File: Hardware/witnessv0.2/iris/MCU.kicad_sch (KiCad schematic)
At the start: 36 parts, among them J1 Conn_01x02, J4 Conn_01x02, U1 ESP32-S3FN8, U8 W25N01KVZEIR, Y1 F322540MUBCE2O

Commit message: iris rework
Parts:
- removed C28, C29: 100n, Capacitor_SMD:C_0402_1005Metric, symbol Device:C_Small
- removed L4: 10n, Inductor_SMD:L_0805_2012Metric, symbol Device:L_Small
- BZ1: footprint Buzzer_Beeper:Buzzer_Murata_PKMCS0909E -> Witness:OWMB-505020S-40-12D
- U8: LCSC_Part (none) -> C22472329
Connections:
- net SPI3_IO2 is gone; now on net SPI2_IO1: U8.2 (DO/IO_{1})
- net +3V3: now also U1.2 (VDD3P3), U1.3 (VDD3P3)
- net BUZZER: now also U1.36 (SPICLK_N)
- net FLASH_CS: now also U1.15 (GPIO10)
- net GND: now also U8.9 (EP)
- net LED_B: now also U1.37 (SPICLK_P)
- net LED_G: now also U1.48 (MTMS)
- net LED_R: now also U1.47 (MTDI)
- net SPI2_CLK: now also U1.17 (GPIO12)
- net SPI2_IO1: now also U1.18 (GPIO13); no longer U8.5 (DI/IO_{0})
- net RXD_MCU: now reaches U1.10 (GPIO5)
- net RAD_RST: now reaches U1.11 (GPIO6)
- net LSM_INT1: now reaches U1.12 (GPIO7)
- net LSM_INT2: now reaches U1.13 (GPIO8)
- net SPI2_IO3: now reaches U1.14 (GPIO9)
- net SPI2_IO3: now also U8.7 (~{HOLD}/~{RESET}/IO_{3})
- net SPI2_IO0: now reaches U1.16 (GPIO11)
- net SPI2_IO0: now also U8.5 (DI/IO_{0})
- net SPI2_IO2: now reaches U1.19 (GPIO14)
- net SPI2_IO2: now also U8.3 (~{WP}/IO_{2})
- net SPI3_SCLK: now reaches U1.21 (XTAL_32K_P)
- net RAD_CS: now reaches U1.22 (XTAL_32K_N)
- net SPI3_COPI: now reaches U1.23 (GPIO17)
- net SPI3_CIPO: now reaches U1.24 (GPIO18)
- net MS56_CS: now reaches U1.27 (GPIO21)
- net I2C_SDA: now reaches U1.38 (GPIO33)
- net I2C_SCL: now reaches U1.39 (GPIO34)
- net LSM_CS: now reaches U1.40 (GPIO35)
- net CANTX: now reaches U1.41 (GPIO36)
- net CANRX: now reaches U1.42 (GPIO37)
- net GPIO: now reaches U1.43 (GPIO38)
- net RAD_BUSY: now reaches U1.44 (MTCK)
- net RAD_RF_EN: now reaches U1.45 (MTDO)
- net VSENSE: now reaches U1.6 (GPIO1)
- net RAD_DIO1: now reaches U1.7 (GPIO2)
- net TXD_MCU: now reaches U1.9 (GPIO4)
- removed net SPI3_IO3: U8.3 (~{WP}/IO_{2}), U8.7 (~{HOLD}/~{RESET}/IO_{3})
- no-connect marks 7 -> 10
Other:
- moved on the sheet: C35, R30, R31

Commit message: trying to make cam board
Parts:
- removed AE1: Antenna_Shield, Connector_Coaxial:U.FL_Molex_MCRF_73412-0110_Vertical, symbol Device:Antenna_Shield
- removed C32, C33, C35: 100n, Capacitor_SMD:C_0402_1005Metric, symbol Device:C_Small
- removed L5: L_Small, Inductor_SMD:L_0402_1005Metric, symbol Device:L_Small
- removed U8: W25N01KVZEIR, Package_SON:WSON-8-1EP_8x6mm_P1.27mm_EP3.4x4.3mm, symbol Witness:W25N01KVZEIR
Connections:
- net FLASH_CS: no longer names the net of U1.15 (GPIO10)
- net GPIO: no longer names the net of U1.43 (GPIO38)
- net RAD_BUSY: no longer names the net of U1.44 (MTCK)
- net RAD_RF_EN: no longer names the net of U1.45 (MTDO)
- net SPI2_CLK: no longer names the net of U1.17 (GPIO12)
- net SPI2_IO0: no longer names the net of U1.16 (GPIO11)
- net SPI2_IO1: no longer names the net of U1.18 (GPIO13)
- net SPI2_IO2: no longer names the net of U1.19 (GPIO14)
- net SPI2_IO3: no longer names the net of U1.14 (GPIO9)

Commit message: lots of iris work
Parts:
- removed U1: ESP32-S3FN8, Package_DFN_QFN:QFN-56-1EP_7x7mm_P0.4mm_EP4x4mm, symbol MCU_Espressif:ESP32-S3
- added U7: ESP32-C3, Package_DFN_QFN:QFN-32-1EP_5x5mm_P0.5mm_EP3.7x3.7mm, symbol MCU_Espressif:ESP32-C3
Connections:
- net +3V3: now also U7.11 (VDD3P3_RTC), U7.17 (VDD3P3_CPU), U7.18 (VDD_SPI), U7.2 (VDD3P3), U7.3 (VDD3P3), U7.31 (VDDA), U7.32 (VDDA)
- net GND: now also U7.33 (GND)
- net RST: now also U7.7 (CHIP_EN)
- net VSENSE: now also U7.6 (GPIO2)
- net XIN: now also U7.30 (XTAL_P)
- new net CS1: U7.4 (XTAL_32K_P)
- new net CS2: U7.5 (XTAL_32K_N)
- new net CS3: U7.8 (GPIO3)
- new net CS4: U7.9 (MTMS)
- no-connect marks 10 -> 4
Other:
- moved on the sheet: C26, C27, C3, C30, C31, C4, C5, C6, R30, R31

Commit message: push for andrew
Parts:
- removed BZ1: Buzzer, Witness:OWMB-505020S-40-12D, symbol Device:Buzzer
- removed R26, R27, R28, R29: 4.7k, Resistor_SMD:R_0402_1005Metric, symbol Device:R_Small
- R24: now not fitted
- R25: now fitted
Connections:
- net CS1 is gone; now on net VSENSE: U7.4 (XTAL_32K_P)
- net CS2 is gone; now on net CANTX: U7.5 (XTAL_32K_N)
- net CS3 is gone; now on net CANRX: U7.8 (GPIO3)
- net CS4 is gone; now on net SDA: U7.9 (MTMS)
- net GPIO46 is gone; now on net BUZZER: R24.2, R25.1
- net LED_B: now also U7.16 (GPIO10)
- net LED_G: now also U7.15 (GPIO9)
- net LED_R: now also U7.6 (GPIO2)
- net RXD1_MCU: now also U7.13 (MTDO)
- net SCL: now also U7.10 (MTDI)
- net TXD1_MCU: now also U7.12 (MTCK)
- net VSENSE: no longer U7.6 (GPIO2)
- net at R30.2: now also U7.25 (GPIO18)
- net at R31.2: now also U7.26 (GPIO19)
- net BUTTON: now reaches U7.14 (GPIO8)
- net RXD0_MCU: now reaches U7.27 (U0RXD)
- net TXD0_MCU: now reaches U7.28 (U0TXD)
- net GPIO0 renamed GPIO9
- no-connect marks 4 -> 8
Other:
- moved on the sheet: R30, R31

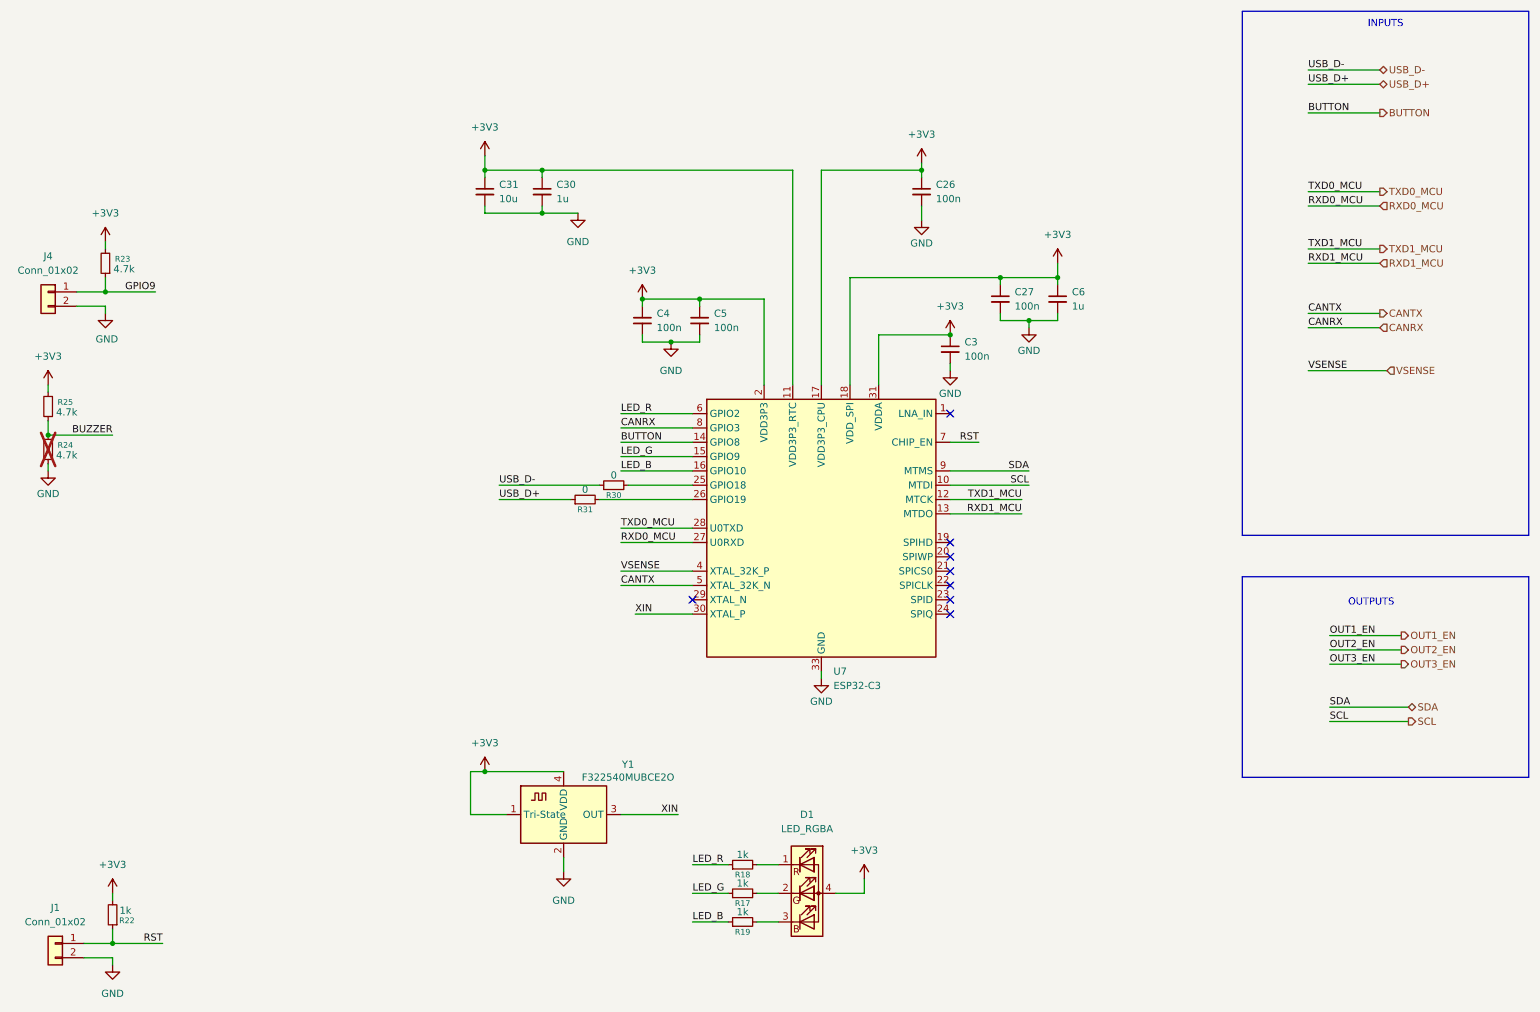
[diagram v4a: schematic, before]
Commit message: i2c io expander and repinning things
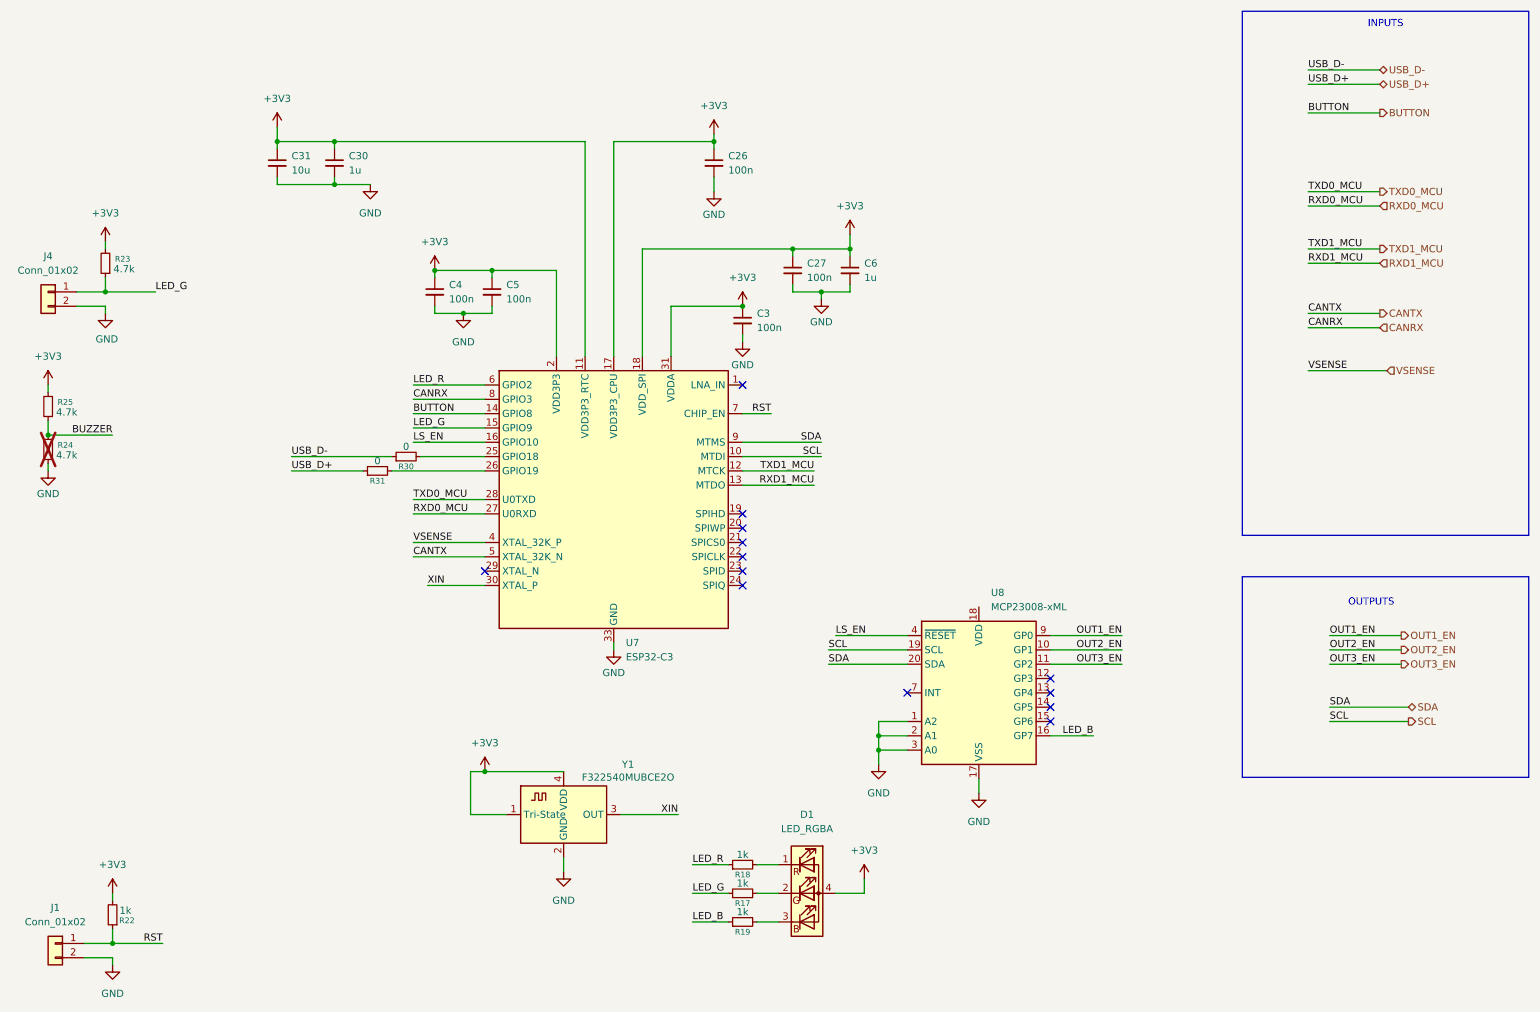
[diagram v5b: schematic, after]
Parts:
- added U8: MCP23008-xML, Package_SO:SO-20_5.3x12.6mm_P1.27mm, symbol Interface_Expansion:MCP23008-xML
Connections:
- net GPIO9 is gone; now on net LED_G: J4.1 (Pin_1), R23.1
- net GND: now also U8.1 (A2), U8.17 (VSS), U8.2 (A1), U8.3 (A0)
- net LED_B: now also U8.16 (GP7); no longer U7.16 (GPIO10)
- net OUT1_EN: now also U8.9 (GP0)
- net OUT2_EN: now also U8.10 (GP1)
- net OUT3_EN: now also U8.11 (GP2)
- net SCL: now also U8.19 (SCL)
- net SDA: now also U8.20 (SDA)
- new net LS_EN: U7.16 (GPIO10), U8.4 (~{RESET})
- no-connect marks 8 -> 13
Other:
- moved on the sheet: C26, C27, C3, C30, C31, C4, C5, C6, R30, R31, U7

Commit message: iris inital layout
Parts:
- removed C30: 1u, Capacitor_SMD:C_0402_1005Metric, symbol Device:C_Small
- removed C31: 10u, Capacitor_SMD:C_0603_1608Metric, symbol Device:C_Small
- removed R24, R25: 4.7k, Resistor_SMD:R_0402_1005Metric, symbol Device:R_Small
- removed U8: MCP23008-xML, Package_SO:SO-20_5.3x12.6mm_P1.27mm, symbol Interface_Expansion:MCP23008-xML
- added C9: 100n, Capacitor_SMD:C_0402_1005Metric, symbol Device:C_Small
- added R42, R45: 1k, Resistor_SMD:R_0402_1005Metric, symbol Device:R_Small
- added R55: 10k, Resistor_SMD:R_0402_1005Metric, symbol Device:R_Small
- added U4: MCP23008-xML, Package_DFN_QFN:QFN-20-1EP_4x4mm_P0.5mm_EP2.7x2.7mm, symbol Interface_Expansion:MCP23008-xML
- U7: value ESP32-C3 -> ESP32-C3FH4
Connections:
- net +3V3: now also C9.1, R42.2, R45.2, U4.18 (VDD)
- net BUTTON: now also U7.6 (GPIO2); no longer U7.14 (GPIO8)
- net GND: now also C9.2, R55.1, U4.1 (A2), U4.17 (VSS), U4.2 (A1), U4.3 (A0)
- net LED_B: now also U4.16 (GP7)
- net LED_R: now also U7.14 (GPIO8); no longer U7.6 (GPIO2)
- net LS_EN: now also R55.2, U4.4 (~{RESET})
- net OUT1_EN: now also U4.9 (GP0)
- net OUT2_EN: now also U4.10 (GP1)
- net OUT3_EN: now also U4.11 (GP2)
- net SCL: now also R45.1, U4.19 (SCL)
- net SDA: now also R42.1, U4.20 (SDA)
- new net 5V_EN: U4.12 (GP3)
- no-connect marks 13 -> 12
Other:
- moved on the sheet: C3

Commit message: routed
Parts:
- added C29, C30: 100n, Capacitor_SMD:C_0402_1005Metric, symbol Device:C_Small
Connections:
- net +3V3: now also C29.1, C30.1
- net GND: now also C29.2, C30.2
- net LED_G: now also U7.16 (GPIO10); no longer U7.15 (GPIO9)
- net LS_EN: now also U7.15 (GPIO9); no longer U7.16 (GPIO10)

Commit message: root feedback
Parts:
- added R24: 4.7k, Resistor_SMD:R_0402_1005Metric, symbol Device:R_Small
- R55: LCSC_Part (none) -> C25744
- U4: LCSC_Part (none) -> C623183
- U7: LCSC_Part (none) -> C2858491
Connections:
- net +3V3: now also R24.2
- net BUTTON: now also R24.1
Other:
- moved on the sheet: J4, R23
